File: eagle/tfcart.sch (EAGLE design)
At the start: 19 parts, among them CN1 MSX_CART, IC7 AT27C020-55JUPLCCS32, IC8 LM1117MPX-3.3

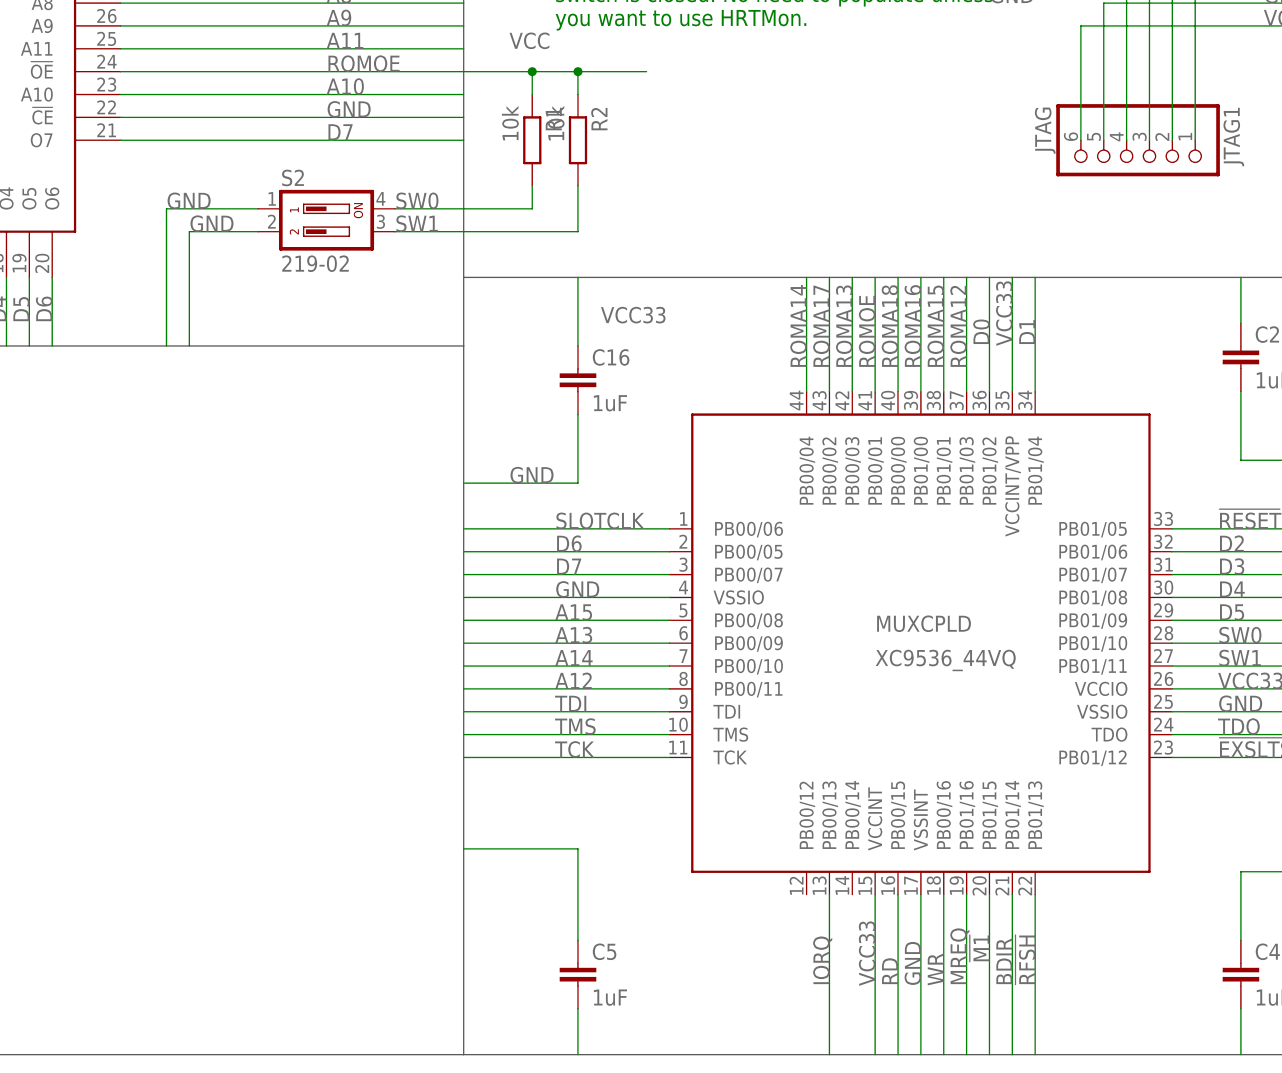
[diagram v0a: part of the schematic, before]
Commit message: MSX Cartridge v1.0 - Complete CPLD-based MegaROM implementation
A minimalist MSX cartridge design based on Xilinx XC9536XL CPLD with
complete build automation and manufacturing outputs.

NOTE: This project has been superseded by RISKYMSX. For new builds,
please use https://github.com/arkadiuszmakarenko/RISKYMSX which offers
superior features including USB ROM loading, SCC emulation, and better
user experience.

Features:
- Xilinx XC9536XL CPLD implementing standard MegaROM mapper
- 4 switchable ROM pages (8KB each) for up to 512KB ROMs
- Docker-based automated build system
- Complete PCB manufacturing pipeline (Gerbers, BOM, CPL, PDF)
- GitHub Actions CI/CD workflows
- GPL v3 licensed hardware and HDL

Build System:
- Docker containers for reproducible builds
- Automated firmware compilation with git versioning
- Eagle CAM processing for PCB manufacturing
- BOM/CPL extraction for assembly
- Automated release packaging

GitHub Actions Workflows:
- Firmware build (CPLD synthesis)
- Gerber generation (PCB fabrication files)
- Assembly file generation (BOM and CPL)
- Schematic PDF generation
- Complete release packaging

Manufacturing:
- 4-layer PCB design optimized for JLCPCB
- Automated Gerber generation via Eagle CAM
- Python scripts for BOM/CPL extraction
- Complete documentation for assembly

License: GNU General Public License v3.0
Copyright (C) 2021-2025 Stephen J. Leary

Build system based on tf536_public project structure.
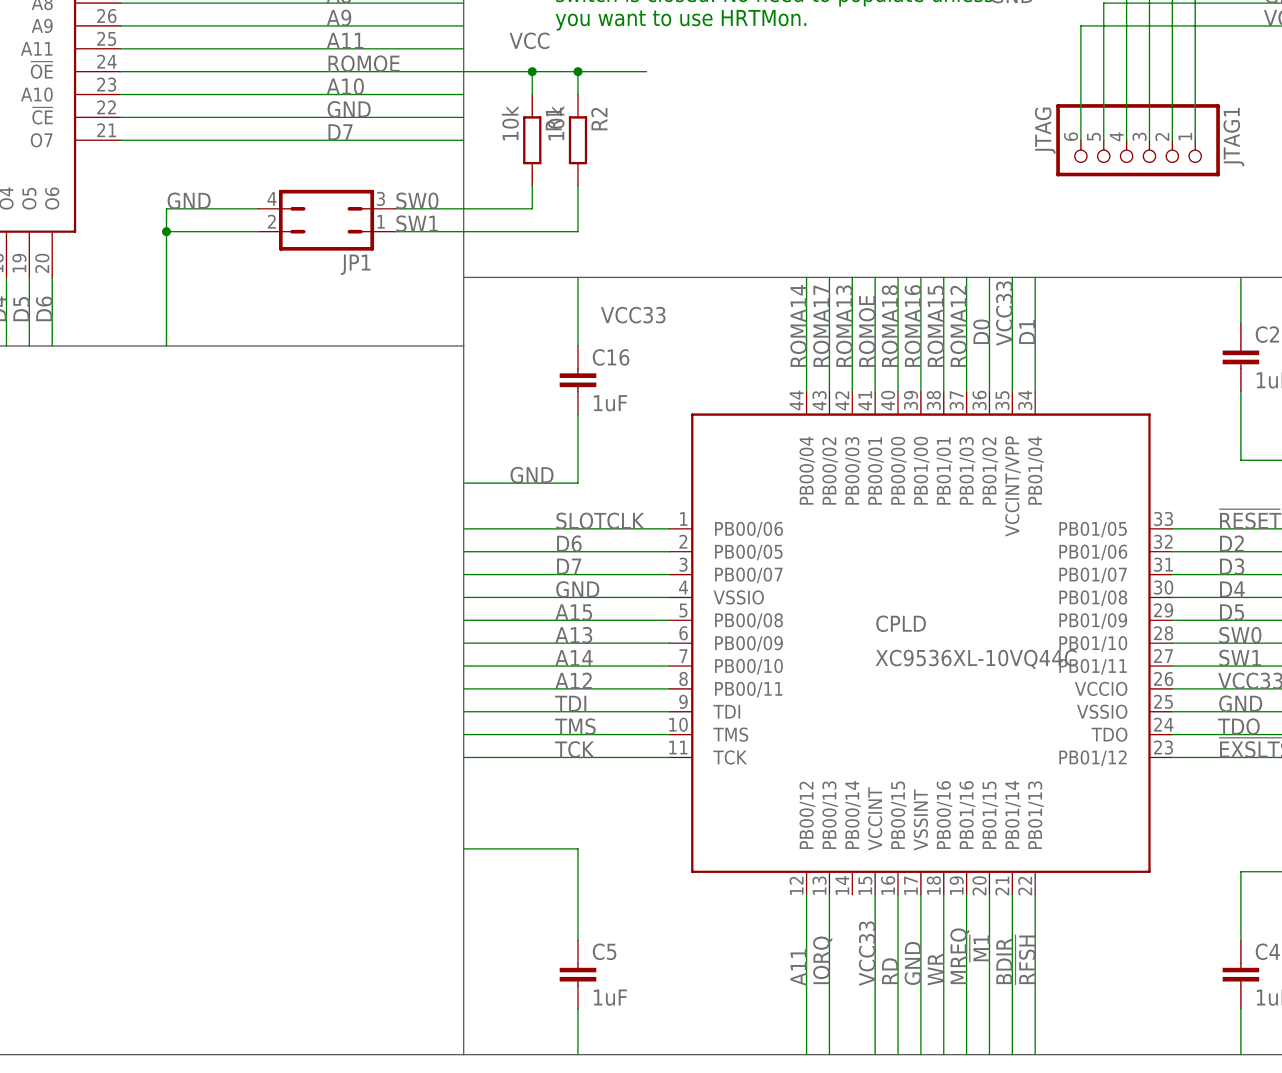
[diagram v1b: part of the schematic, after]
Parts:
- removed S2: 219-02, switch-dil:219-02
- added JP1: (no value), jumper:JP2Q
- CPLD: value XC9536_44VQ -> XC9536XL-10VQ44C
- renumbered MUXCPLD to CPLD
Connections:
- net A11: now also CPLD.PB00/12
- net GND: now also JP1.2, JP1.4; no longer S2.1, S2.2
- net SW0: now also JP1.3; no longer S2.4
- net SW1: now also JP1.1; no longer S2.3

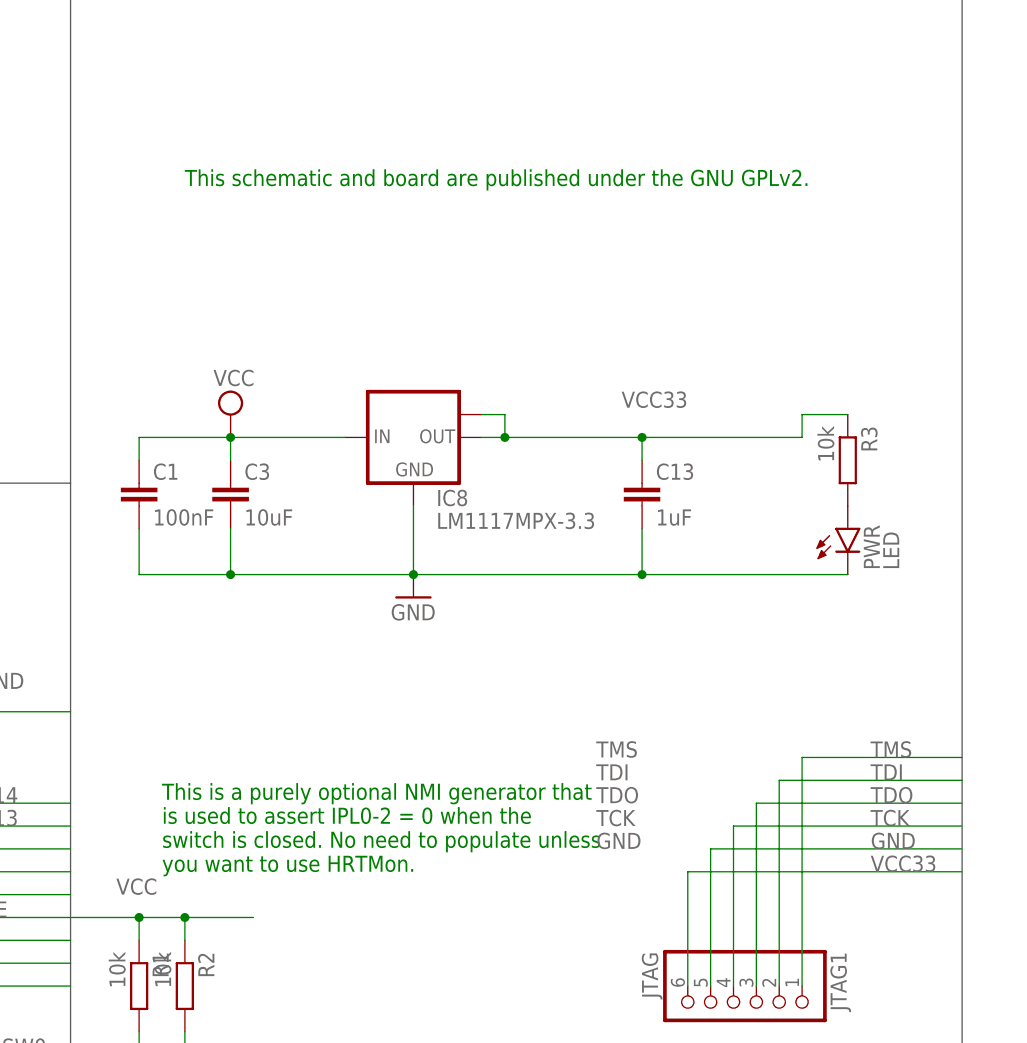
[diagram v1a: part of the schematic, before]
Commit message: removed redundant text from schematic
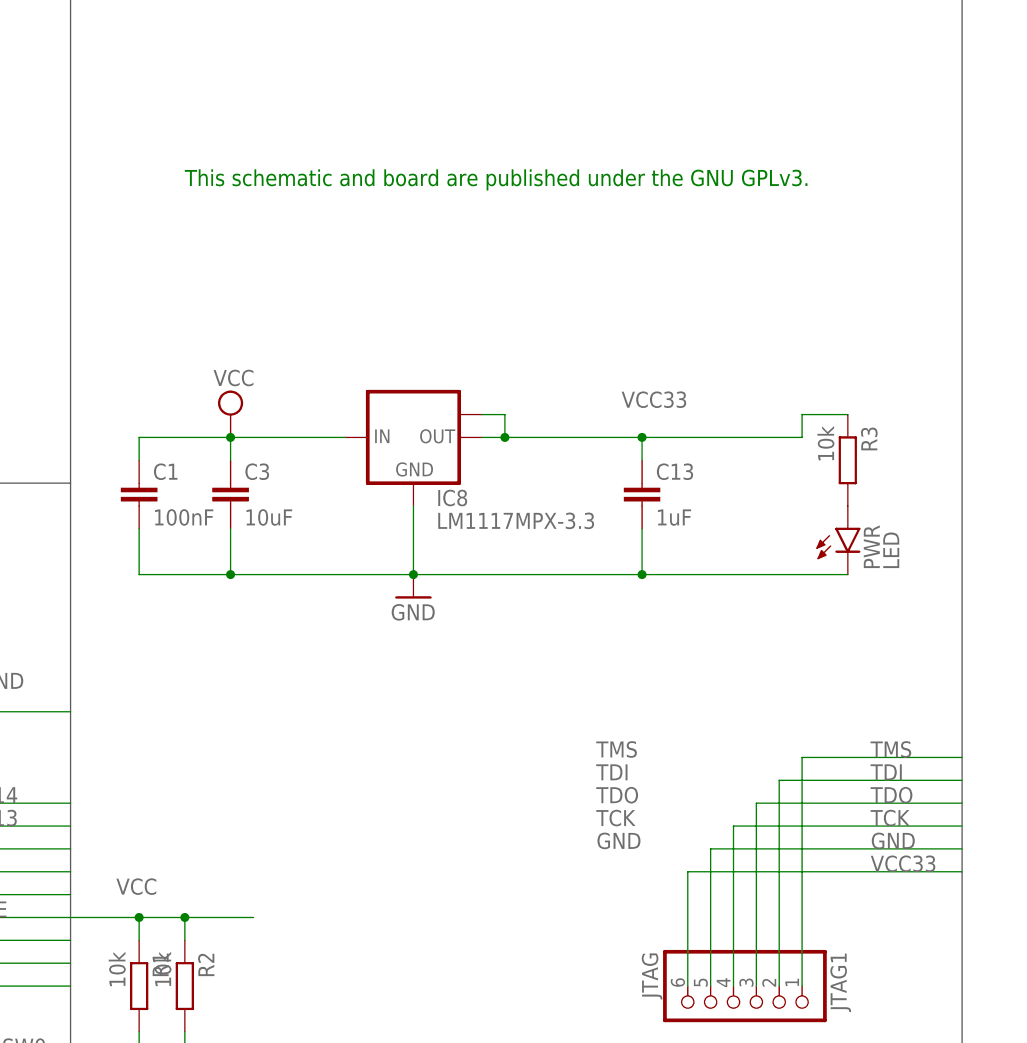
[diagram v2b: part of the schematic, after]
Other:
- note added: "This schematic and board are published under the GNU GPLv3."
- note removed: "This is a purely optional NMI generator that is used to assert IPL0-2 = 0 when the switch is closed. No need to populate unless you want to use HRTMon."
- note removed: "This schematic and board are published under the GNU GPLv2."
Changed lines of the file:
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@@
 <sheet>
 <plain>
-<text x="177.8" y="114.3" size="1.778" layer="91">This is a purely optional NMI generator that
-is used to assert IPL0-2 = 0 when the
-switch is closed. No need to populate unless
-you want to use HRTMon.</text>
-<text x="180.34" y="190.5" size="1.778" layer="91">This schematic and board are published under the GNU GPLv2. </text>
+<text x="180.34" y="190.5" size="1.778" layer="91">This schematic and board are published under the GNU GPLv3. </text>
 </plain>
 <instances>
@@
 </drawing>
 <compatibility>
-<note version="6.3" minversion="6.2.2" severity="warning">
-Since Version 6.2.2 text objects can contain more than one line,
-which will not be processed correctly with this version.
-</note>
 <note version="8.2" severity="warning">
 Since Version 8.2, EAGLE supports online libraries. The ids
